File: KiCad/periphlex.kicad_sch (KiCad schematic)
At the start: 14 parts

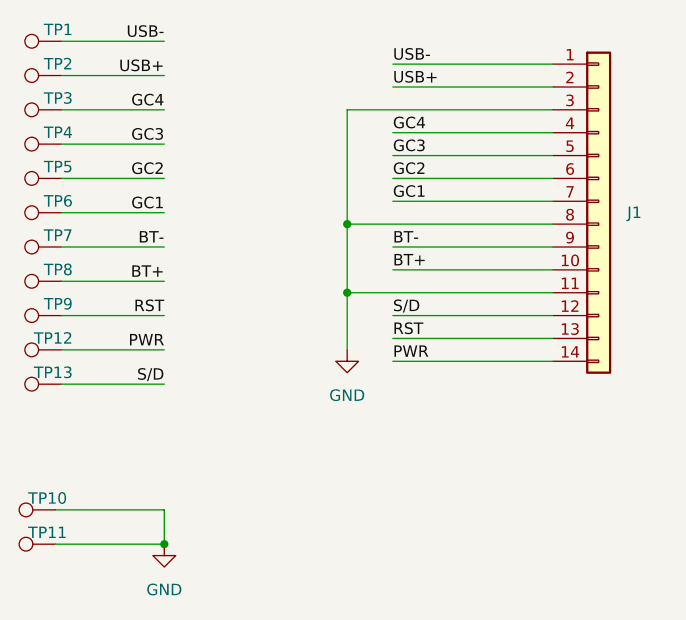
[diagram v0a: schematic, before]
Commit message: Swap shutdown and reset lines on flex for easier routing
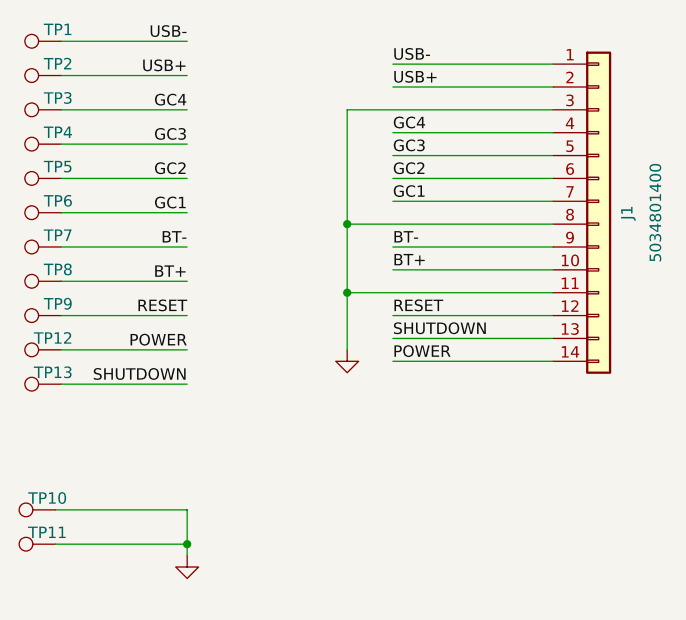
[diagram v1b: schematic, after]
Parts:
- J1: value ~ -> 5034801400
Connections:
- net PWR renamed POWER
- net RST renamed RESET
- net RESET: now also J1.12 (Pin_12); no longer J1.13 (Pin_13)
- net S/D renamed SHUTDOWN
- net SHUTDOWN: now also J1.13 (Pin_13); no longer J1.12 (Pin_12)
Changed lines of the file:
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@@
-	)
-	(junction
-		(at 130.81 133.35)
-		(diameter 0)
-		(color 0 0 0 0)
 	)
 	(junction
@@
 		(color 0 0 0 0)
 	)
-	(wire
-		(pts
-			(xy 118.745 129.54) (xy 130.81 129.54)
-		)
-		(stroke
-			(width 0)
-			(type default)
-		)
-	)
-	(wire
-		(pts
-			(xy 119.38 107.95) (xy 130.81 107.95)
+	(junction
+		(at 133.35 133.35)
+		(diameter 0)
+		(color 0 0 0 0)
+	)
+	(wire
+		(pts
+			(xy 118.745 129.54) (xy 133.35 129.54)
+		)
+		(stroke
+			(width 0)
+			(type default)
+		)
+	)
+	(wire
+		(pts
+			(xy 119.38 107.95) (xy 133.35 107.95)
 		)
 		(stroke
@@
 	(wire
 		(pts
-			(xy 119.38 115.57) (xy 130.81 115.57)
-		)
-		(stroke
-			(width 0)
-			(type default)
-		)
-	)
-	(wire
-		(pts
-			(xy 119.38 77.47) (xy 130.81 77.47)
+			(xy 119.38 115.57) (xy 133.35 115.57)
+		)
+		(stroke
+			(width 0)
+			(type default)
+		)
+	)
+	(wire
+		(pts
+			(xy 119.38 77.47) (xy 133.35 77.47)
 		)
 		(stroke
@@
 	(wire
 		(pts
-			(xy 119.38 96.52) (xy 130.81 96.52)
-		)
-		(stroke
-			(width 0)
-			(type default)
-		)
-	)
-	(wire
-		(pts
-			(xy 119.38 85.09) (xy 130.81 85.09)
+			(xy 119.38 96.52) (xy 133.35 96.52)
+		)
+		(stroke
+			(width 0)
+			(type default)
+		)
+	)
+	(wire
+		(pts
+			(xy 119.38 85.09) (xy 133.35 85.09)
 		)
 		(stroke
@@
 	(wire
 		(pts
+			(xy 133.35 134.62) (xy 133.35 133.35)
+		)
+		(stroke
+			(width 0)
+			(type default)
+		)
+	)
+	(wire
+		(pts
 			(xy 173.99 87.63) (xy 156.21 87.63)
 		)
@@
 	(wire
 		(pts
-			(xy 119.38 100.33) (xy 130.81 100.33)
+			(xy 119.38 100.33) (xy 133.35 100.33)
 		)
 		(stroke
@@
 	(wire
 		(pts
-			(xy 119.38 88.9) (xy 130.81 88.9)
+			(xy 119.38 88.9) (xy 133.35 88.9)
+		)
+		(stroke
+			(width 0)
+			(type default)
+		)
+	)
+	(wire
+		(pts
+			(xy 118.745 133.35) (xy 133.35 133.35)
 		)
 		(stroke
@@
 	(wire
 		(pts
-			(xy 119.38 104.14) (xy 130.81 104.14)
+			(xy 119.38 104.14) (xy 133.35 104.14)
 		)
 		(stroke
@@
 	(wire
 		(pts
-			(xy 119.38 111.76) (xy 130.81 111.76)
+			(xy 119.38 111.76) (xy 133.35 111.76)
 		)
 		(stroke
@@
 	(wire
 		(pts
-			(xy 119.38 81.28) (xy 130.81 81.28)
+			(xy 119.38 81.28) (xy 133.35 81.28)
 		)
 		(stroke
@@
 	(wire
 		(pts
-			(xy 118.745 133.35) (xy 130.81 133.35)
-		)
-		(stroke
-			(width 0)
-			(type default)
-		)
-	)
-	(wire
-		(pts
-			(xy 119.38 92.71) (xy 130.81 92.71)
+			(xy 119.38 92.71) (xy 133.35 92.71)
 		)
 		(stroke
@@
 	(wire
 		(pts
-			(xy 130.81 129.54) (xy 130.81 133.35)
+			(xy 133.35 129.54) (xy 133.35 133.35)
 		)
 		(stroke
@@
 	)
 	(label "GC4"
-		(at 130.81 85.09 180)
+		(at 133.35 85.09 180)
 		(fields_autoplaced yes)
 		(effects
@@
 		)
 	)
-	(label "S{slash}D"
-		(at 156.21 107.95 0)
+	(label "SHUTDOWN"
+		(at 156.21 110.49 0)
 		(fields_autoplaced yes)
 		(effects
@@
 	)
 	(label "GC2"
-		(at 130.81 92.71 180)
+		(at 133.35 92.71 180)
 		(fields_autoplaced yes)
 		(effects
@@
 	)
 	(label "USB-"
-		(at 130.81 77.47 180)
+		(at 133.35 77.47 180)
 		(fields_autoplaced yes)
 		(effects
@@
 	)
 	(label "GC3"
-		(at 130.81 88.9 180)
+		(at 133.35 88.9 180)
 		(fields_autoplaced yes)
 		(effects
@@
 		)
 	)
-	(label "S{slash}D"
-		(at 130.81 115.57 180)
+	(label "SHUTDOWN"
+		(at 133.35 115.57 180)
 		(fields_autoplaced yes)
 		(effects
@@
 		)
 	)
-	(label "RST"
-		(at 130.81 107.95 180)
+	(label "RESET"
+		(at 133.35 107.95 180)
 		(fields_autoplaced yes)
 		(effects
@@
 		)
 	)
-	(label "RST"
-		(at 156.21 110.49 0)
+	(label "RESET"
+		(at 156.21 107.95 0)
 		(fields_autoplaced yes)
 		(effects
@@
 	)
 	(label "BT+"
-		(at 130.81 104.14 180)
+		(at 133.35 104.14 180)
 		(fields_autoplaced yes)
 		(effects
@@
 	)
 	(label "USB+"
-		(at 130.81 81.28 180)
+		(at 133.35 81.28 180)
 		(fields_autoplaced yes)
 		(effects
@@
 	)
 	(label "GC1"
-		(at 130.81 96.52 180)
+		(at 133.35 96.52 180)
 		(fields_autoplaced yes)
 		(effects
@@
 		)
 	)
-	(label "PWR"
+	(label "POWER"
 		(at 156.21 113.03 0)
 		(fields_autoplaced yes)
@@
 	)
 	(label "BT-"
-		(at 130.81 100.33 180)
+		(at 133.35 100.33 180)
 		(fields_autoplaced yes)
 		(effects
@@
 		)
 	)
-	(label "PWR"
-		(at 130.81 111.76 180)
+	(label "POWER"
+		(at 133.35 111.76 180)
 		(fields_autoplaced yes)
 		(effects
@@
 		)
 		(instances
-			(project "wii-peripheral-flex"
+			(project "periphlex"
 				(path "/b8879ac1-19e5-471c-81b5-561e601c2849"
 					(reference "TP2")
@@
 		)
 		(instances
-			(project "wii-peripheral-flex"
+			(project "periphlex"
 				(path "/b8879ac1-19e5-471c-81b5-561e601c2849"
 					(reference "TP11")
@@
 		)
 		(instances
-			(project "wii-peripheral-flex"
+			(project "periphlex"
 				(path "/b8879ac1-19e5-471c-81b5-561e601c2849"
 					(reference "TP12")
@@
 		)
 		(instances
-			(project "wii-peripheral-flex"
+			(project "periphlex"
 				(path "/b8879ac1-19e5-471c-81b5-561e601c2849"
 					(reference "TP7")
@@
 		)
 		(instances
-			(project "wii-peripheral-flex"
+			(project "periphlex"
 				(path "/b8879ac1-19e5-471c-81b5-561e601c2849"
 					(reference "TP1")
@@
 					(size 1.27 1.27)
 				)
+				(hide yes)
 			)
 		)
@@
 		)
 		(instances
-			(project "wii-peripheral-flex"
+			(project "periphlex"
 				(path "/b8879ac1-19e5-471c-81b5-561e601c2849"
 					(reference "#PWR01")
@@
 		)
 		(instances
-			(project "wii-peripheral-flex"
+			(project "periphlex"
 				(path "/b8879ac1-19e5-471c-81b5-561e601c2849"
 					(reference "TP6")
@@
 		)
 		(instances
-			(project "wii-peripheral-flex"
+			(project "periphlex"
 				(path "/b8879ac1-19e5-471c-81b5-561e601c2849"
 					(reference "TP4")
@@
 	(symbol
 		(lib_id "power:GND")
-		(at 130.81 133.35 0)
+		(at 133.35 134.62 0)
 		(unit 1)
 		(exclude_from_sim no)
@@
 		(fields_autoplaced yes)
 		(property "Reference" "#PWR02"
-			(at 130.81 139.7 0)
+			(at 133.35 140.97 0)
 			(effects
 				(font
@@
 		)
 		(property "Value" "GND"
-			(at 130.81 138.43 0)
-			(effects
-				(font
-					(size 1.27 1.27)
-				)
+			(at 133.35 139.7 0)
+			(effects
+				(font
+					(size 1.27 1.27)
+				)
+				(hide yes)
 			)
 		)
 		(property "Footprint" ""
-			(at 130.81 133.35 0)
+			(at 133.35 134.62 0)
 			(effects
 				(font
@@
 		)
 		(property "Datasheet" ""
-			(at 130.81 133.35 0)
+			(at 133.35 134.62 0)
 			(effects
 				(font
@@
 		)
 		(property "Description" ""
-			(at 130.81 133.35 0)
+			(at 133.35 134.62 0)
 			(effects
 				(font
@@
 		)
 		(instances
-			(project "wii-peripheral-flex"
+			(project "periphlex"
 				(path "/b8879ac1-19e5-471c-81b5-561e601c2849"
 					(reference "#PWR02")
@@
 		)
 		(instances
-			(project "wii-peripheral-flex"
+			(project "periphlex"
 				(path "/b8879ac1-19e5-471c-81b5-561e601c2849"
 					(reference "TP10")
@@
 		(on_board yes)
 		(dnp no)
-		(fields_autoplaced yes)
 		(property "Reference" "J1"
-			(at 182.245 96.5199 0)
-			(effects
-				(font
-					(size 1.27 1.27)
-				)
-				(justify left)
-			)
-		)
-		(property "Value" "~"
+			(at 182.245 96.5199 90)
+			(effects
+				(font
+					(size 1.27 1.27)
+				)
+			)
+		)
+		(property "Value" "5034801400"
 			(at 185.42 96.52 90)
 			(effects
@@
 					(size 1.27 1.27)
 				)
-				(hide yes)
 			)
 		)
@@
 		)
 		(instances
-			(project "wii-peripheral-flex"
+			(project "periphlex"
 				(path "/b8879ac1-19e5-471c-81b5-561e601c2849"
 					(reference "J1")
@@
 		)
 		(instances
-			(project "wii-peripheral-flex"
+			(project "periphlex"
 				(path "/b8879ac1-19e5-471c-81b5-561e601c2849"
 					(reference "TP3")
@@
 		)
 		(instances
-			(project "wii-peripheral-flex"
+			(project "periphlex"
 				(path "/b8879ac1-19e5-471c-81b5-561e601c2849"
 					(reference "TP8")
@@
 		)
 		(instances
-			(project "wii-peripheral-flex"
+			(project "periphlex"
 				(path "/b8879ac1-19e5-471c-81b5-561e601c2849"
 					(reference "TP5")
@@
 		)
 		(instances
-			(project "wii-peripheral-flex"
+			(project "periphlex"
 				(path "/b8879ac1-19e5-471c-81b5-561e601c2849"
 					(reference "TP9")
@@
 		)
 		(instances
-			(project "wii-peripheral-flex"
+			(project "periphlex"
 				(path "/b8879ac1-19e5-471c-81b5-561e601c2849"
 					(reference "TP13")
